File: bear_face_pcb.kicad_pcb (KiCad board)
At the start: 2 copper layers, 300 x 111.8 mm, 216 parts, among them J1 USB-C, J2 Conn_02x03_Odd_Even, SW1 RESET, U1 ATmega32U4-AU, U2 SRV05-4, Y1 16MHz

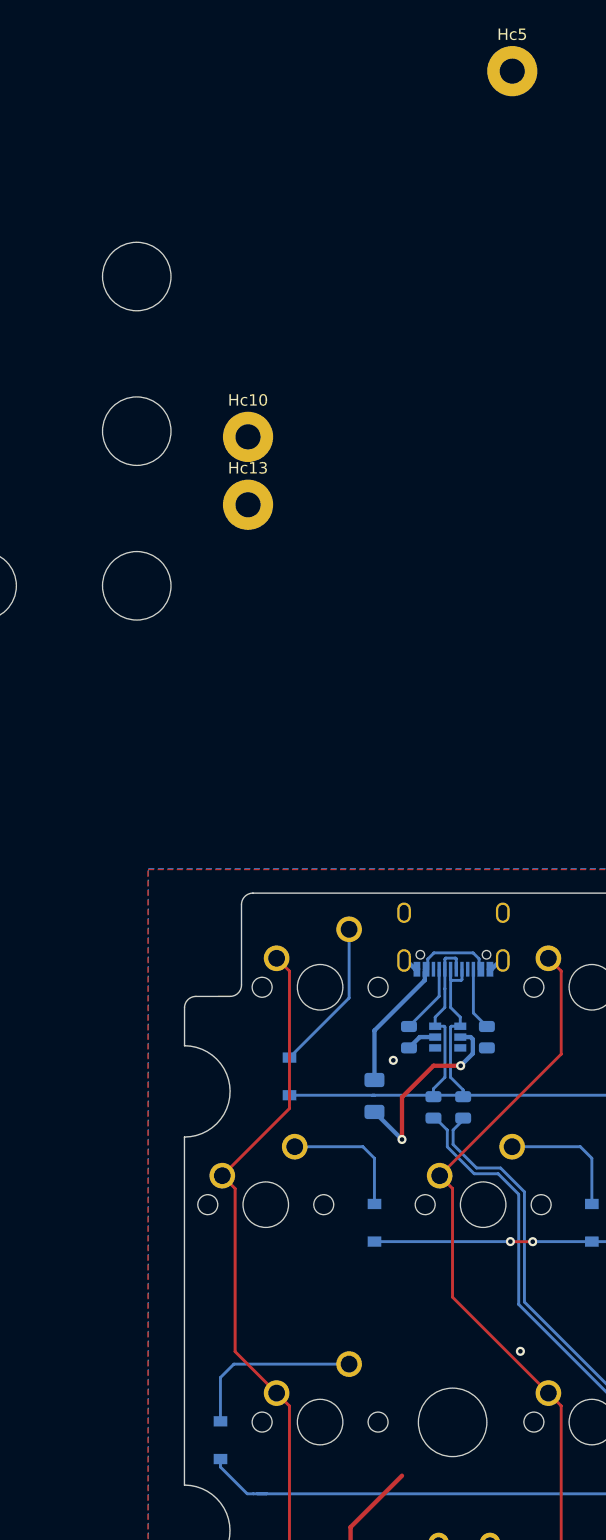
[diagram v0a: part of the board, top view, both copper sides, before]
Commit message: softened corners * mount holes still WIP
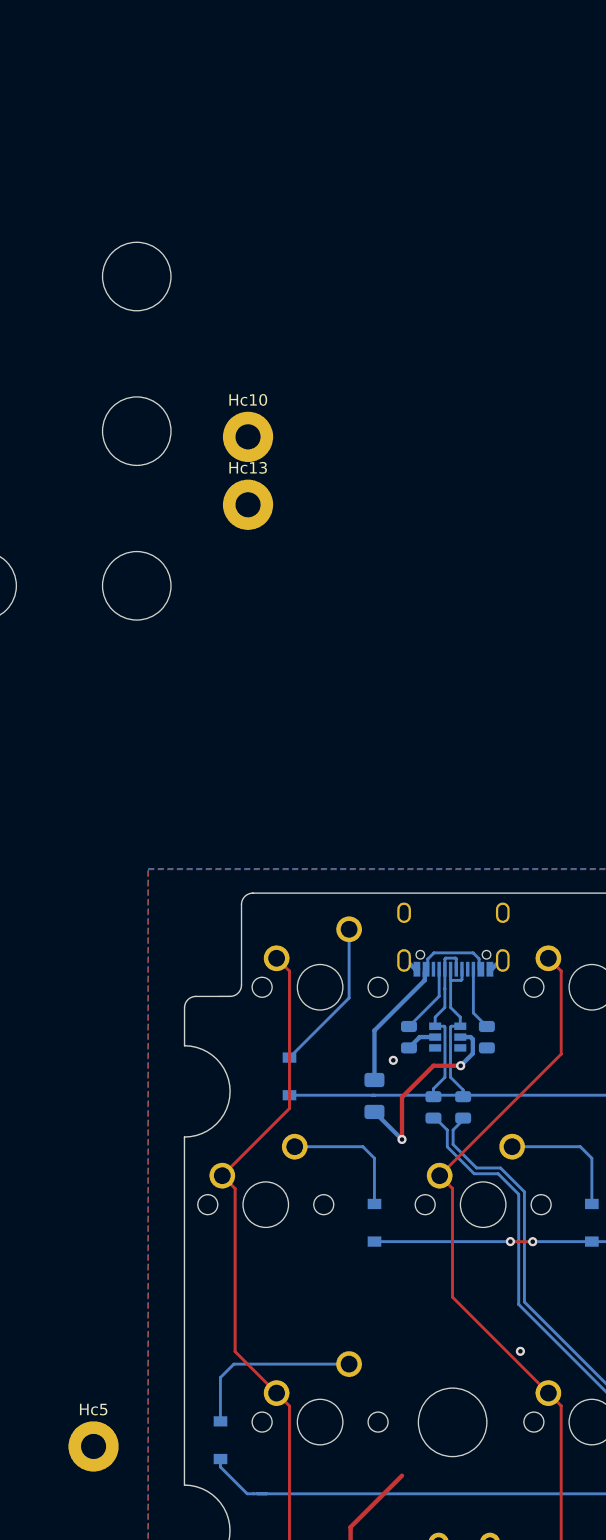
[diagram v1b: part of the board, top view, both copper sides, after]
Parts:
- moved Hc5 126.0 mm to (52.3, 118.1)
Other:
- board text removed: "USB CUTOUT"
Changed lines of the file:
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@@
   )
   (footprint "MountingHole:MountingHole_2.2mm_M2_Pad" (layer "F.Cu")
-    (at 89.037 -2.424)
+    (at 52.3494 118.0846)
     (descr "Mounting Hole 2.2mm, M2")
     (tags "mounting hole 2.2mm m2")
@@
     (fp_circle (center 0 0) (end 2.45 0)
       (stroke (width 0.05) (type solid)) (fill none) (layer "F.CrtYd"))
-    (pad "1" thru_hole circle (at 0 0) (size 4.4 4.4) (drill 2.2) (layers "*.Cu" "*.Mask")
+    (pad "1" thru_hole circle (at 0 0) (size 4.4 4.4) (drill 2.2) (layers "*.Cu" "B.Mask")
       (net 84 "GND") (pinfunction "Pin_1") (pintype "passive"))
   )
@@
     )
     (fp_line (start -4.468987 -5.094056) (end -4.468987 -3.612751)
-      (stroke (width 0.254001) (type solid)) (layer "B.SilkS"))
+      (stroke (width 0.254) (type solid)) (layer "B.SilkS"))
     (fp_line (start -4.468987 -1.375667) (end -4.468987 0.487249)
-      (stroke (width 0.254001) (type solid)) (layer "B.SilkS"))
+      (stroke (width 0.254) (type solid)) (layer "B.SilkS"))
     (fp_line (start 4.471019 -5.094056) (end -4.468987 -5.094056)
-      (stroke (width 0.254001) (type solid)) (layer "B.SilkS"))
+      (stroke (width 0.254) (type solid)) (layer "B.SilkS"))
     (fp_line (start 4.471019 -5.094056) (end 4.471019 -3.612395)
-      (stroke (width 0.254001) (type solid)) (layer "B.SilkS"))
+      (stroke (width 0.254) (type solid)) (layer "B.SilkS"))
     (fp_line (start 4.471019 -1.376022) (end 4.471019 0.487605)
-      (stroke (width 0.254001) (type solid)) (layer "B.SilkS"))
+      (stroke (width 0.254) (type solid)) (layer "B.SilkS"))
     (fp_circle (center -4.475032 2.75616) (end -4.445034 2.75616)
       (stroke (width 0.059995) (type solid)) (fill none) (layer "B.SilkS"))
     (fp_circle (center -2.899924 1.205664) (end -2.774956 1.205664)
-      (stroke (width 0.250013) (type solid)) (fill none) (layer "B.Fab"))
+      (stroke (width 0.250012) (type solid)) (fill none) (layer "B.Fab"))
     (fp_circle (center 2.899924 1.205664) (end 3.024892 1.205664)
-      (stroke (width 0.250013) (type solid)) (fill none) (layer "B.Fab"))
+      (stroke (width 0.250012) (type solid)) (fill none) (layer "B.Fab"))
     (pad "" np_thru_hole circle (at -2.899924 1.205664) (size 0.750013 0.750013) (drill 0.750013) (layers "*.Cu" "*.Mask"))
     (pad "" np_thru_hole circle (at 2.899924 1.205664) (size 0.750013 0.750013) (drill 0.750013) (layers "*.Cu" "*.Mask"))
@@
     )
   )
-  (gr_line (start 364.2995 65.94475) (end 364.2995 185.00725)
-    (stroke (width 0.15) (type solid)) (layer "Cmts.User"))
-  (gr_line (start 56.3245 185.00725) (end 364.2995 185.00725)
-    (stroke (width 0.15) (type solid)) (layer "Cmts.User"))
   (gr_line (start 79.68 69.866) (end 88.062 69.866)
     (stroke (width 0.15) (type solid)) (layer "Cmts.User"))
-  (gr_line (start 56.3245 65.94475) (end 56.3245 185.00725)
-    (stroke (width 0.15) (type solid)) (layer "Cmts.User"))
-  (gr_line (start 56.3245 65.94475) (end 364.2995 65.94475)
-    (stroke (width 0.15) (type solid)) (layer "Cmts.User"))
-  (gr_line (start 88.182 68.676) (end 90.212 63.376)
-    (stroke (width 0.15) (type solid)) (layer "Cmts.User"))
   (gr_line (start 65.361515 181.447) (end 355.240091 181.447)
     (stroke (width 0.12) (type solid)) (layer "Edge.Cuts"))
@@
     (effects (font (size 1.5 1.5) (thickness 0.3)) (justify mirror))
   )
-  (gr_text "USB CUTOUT" (at 95.002 63.436) (layer "Cmts.User")
-    (effects (font (size 1 1) (thickness 0.15)))
-  )
   (gr_text "CASE OUTLINE" (at 61.512 64.976) (layer "Cmts.User")

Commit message: changing mount holes to unplated WIP
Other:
- outline, holes or cut-outs redrawn
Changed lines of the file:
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@@
   (gr_line (start 354.319106 69.601002) (end 66.312 69.601501)
     (stroke (width 0.12) (type solid)) (layer "Edge.Cuts"))
-  (gr_line (start 60.312 90.976) (end 60.312 121.472447)
+  (gr_line (start 60.312 91.201) (end 60.312 121.226)
     (stroke (width 0.12) (type solid)) (layer "Edge.Cuts"))
-  (gr_line (start 360.312 79.651002) (end 360.312 82.976)
+  (gr_line (start 360.312 79.651002) (end 360.308814 82.725999)
     (stroke (width 0.12) (type solid)) (layer "Edge.Cuts"))
-  (gr_line (start 360.32 90.976) (end 360.3112 121.476)
+  (gr_line (start 360.312 91.222777) (end 360.312 121.236)
     (stroke (width 0.12) (type solid)) (layer "Edge.Cuts"))
-  (gr_line (start 60.312 148.479) (end 60.3128 159.5506)
+  (gr_line (start 60.313777 148.727777) (end 60.312001 159.300999)
     (stroke (width 0.12) (type solid)) (layer "Edge.Cuts"))
-  (gr_arc (start 60.319106 82.976) (mid 64.312005 86.979553) (end 60.312 90.976006)
+  (gr_arc (start 60.563658 83.001106) (mid 64.294852 86.976831) (end 60.562 90.950999)
     (stroke (width 0.12) (type solid)) (layer "Edge.Cuts"))
-  (gr_arc (start 360.312 90.976) (mid 356.312 86.976) (end 360.312 82.976)
+  (gr_arc (start 360.065012 90.975999) (mid 356.304383 86.977504) (end 360.06201 82.976188)
     (stroke (width 0.12) (type solid)) (layer "Edge.Cuts"))
   (gr_arc (start 360.32 176.397485) (mid 358.821399 179.969862) (end 355.240091 181.447)
     (stroke (width 0.12) (type solid)) (layer "Edge.Cuts"))
+  (gr_arc (start 360.064933 167.559147) (mid 360.246694 167.634302) (end 360.322 167.816)
+    (stroke (width 0.12) (type default)) (layer "Edge.Cuts"))
+  (gr_arc (start 60.313777 129.718716) (mid 60.387 129.541939) (end 60.563777 129.468716)
+    (stroke (width 0.12) (type default)) (layer "Edge.Cuts"))
+  (gr_arc (start 60.313777 148.727777) (mid 60.387 148.551) (end 60.563777 148.477777)
+    (stroke (width 0.12) (type default)) (layer "Edge.Cuts"))
+  (gr_arc (start 360.312 159.334239) (mid 360.236845 159.516) (end 360.055147 159.591306)
+    (stroke (width 0.12) (type default)) (layer "Edge.Cuts"))
   (gr_arc (start 354.319106 69.601002) (mid 355.026208 69.893897) (end 355.319106 70.601002)
     (stroke (width 0.12) (type default)) (layer "Edge.Cuts"))
-  (gr_line (start 360.3112 129.476) (end 360.3112 159.576)
+  (gr_arc (start 360.312 121.236) (mid 360.238853 121.412915) (end 360.062 121.486214)
+    (stroke (width 0.12) (type default)) (layer "Edge.Cuts"))
+  (gr_line (start 360.312 129.716) (end 360.312 159.339085)
     (stroke (width 0.12) (type default)) (layer "Edge.Cuts"))
   (gr_arc (start 356.319106 78.65) (mid 355.611995 78.357109) (end 355.319106 77.65)
+    (stroke (width 0.12) (type default)) (layer "Edge.Cuts"))
+  (gr_arc (start 60.562 121.476) (mid 60.385223 121.402777) (end 60.312 121.226)
+    (stroke (width 0.12) (type default)) (layer "Edge.Cuts"))
+  (gr_arc (start 360.065012 90.976) (mid 360.239646 91.048204) (end 360.312 91.222777)
     (stroke (width 0.12) (type default)) (layer "Edge.Cuts"))
   (gr_arc (start 65.361515 181.447826) (mid 61.789129 179.949227) (end 60.312 176.367917)
@@
   (gr_line (start 355.319106 77.65) (end 355.319106 70.601002)
     (stroke (width 0.12) (type default)) (layer "Edge.Cuts"))
-  (gr_arc (start 360.3112 167.576) (mid 356.3112 163.576) (end 360.3112 159.576)
+  (gr_arc (start 360.064933 167.559146) (mid 356.320451 163.580833) (end 360.055286 159.593462)
     (stroke (width 0.12) (type solid)) (layer "Edge.Cuts"))
   (gr_line (start 359.312 78.651002) (end 356.319106 78.65)
@@
   (gr_arc (start 65.312 77.650499) (mid 65.019107 78.357606) (end 64.312 78.650499)
     (stroke (width 0.12) (type default)) (layer "Edge.Cuts"))
-  (gr_arc (start 60.312 140.479) (mid 64.312 144.479) (end 60.312 148.479)
+  (gr_arc (start 60.5634 140.4802) (mid 64.318695 144.478811) (end 60.563777 148.477776)
     (stroke (width 0.12) (type solid)) (layer "Edge.Cuts"))
   (gr_arc (start 60.319106 79.651501) (mid 60.611999 78.944396) (end 61.319106 78.651501)
@@
   (gr_arc (start 65.312 70.601501) (mid 65.604893 69.894394) (end 66.312 69.601501)
     (stroke (width 0.12) (type default)) (layer "Edge.Cuts"))
+  (gr_arc (start 360.308814 82.725999) (mid 360.23673 82.901717) (end 360.06201 82.976188)
+    (stroke (width 0.12) (type default)) (layer "Edge.Cuts"))
   (gr_arc (start 359.312 78.651002) (mid 360.019106 78.943895) (end 360.312 79.651002)
+    (stroke (width 0.12) (type default)) (layer "Edge.Cuts"))
+  (gr_arc (start 60.569106 82.999223) (mid 60.392329 82.926) (end 60.319106 82.749223)
+    (stroke (width 0.12) (type default)) (layer "Edge.Cuts"))
+  (gr_arc (start 60.562001 159.550999) (mid 60.385224 159.477776) (end 60.312001 159.300999)
     (stroke (width 0.12) (type default)) (layer "Edge.Cuts"))
   (gr_line (start 64.312 78.650499) (end 61.319106 78.651501)
     (stroke (width 0.12) (type default)) (layer "Edge.Cuts"))
-  (gr_line (start 60.312 167.5506) (end 60.312 176.367917)
+  (gr_line (start 60.312 167.801) (end 60.312 176.367917)
+    (stroke (width 0.12) (type default)) (layer "Edge.Cuts"))
+  (gr_arc (start 60.563777 140.474223) (mid 60.387 140.401) (end 60.313777 140.224223)
     (stroke (width 0.12) (type default)) (layer "Edge.Cuts"))
   (gr_line (start 65.312 70.601501) (end 65.312 77.650499)
     (stroke (width 0.12) (type default)) (layer "Edge.Cuts"))
-  (gr_arc (start 60.312 121.472447) (mid 64.304899 125.476) (end 60.304894 129.472453)
+  (gr_arc (start 60.56189 121.477707) (mid 64.307872 125.484918) (end 60.537 129.468716)
     (stroke (width 0.12) (type solid)) (layer "Edge.Cuts"))
-  (gr_line (start 60.319106 79.651501) (end 60.319106 82.976)
+  (gr_line (start 60.319106 79.651501) (end 60.319106 82.749223)
     (stroke (width 0.12) (type default)) (layer "Edge.Cuts"))
-  (gr_line (start 360.32 167.576) (end 360.32 176.397485)
+  (gr_line (start 360.322 167.816) (end 360.32 176.397485)
     (stroke (width 0.12) (type default)) (layer "Edge.Cuts"))
-  (gr_line (start 60.312 129.472453) (end 60.312 140.479)
+  (gr_line (start 60.313777 129.718716) (end 60.313777 140.224223)
     (stroke (width 0.12) (type default)) (layer "Edge.Cuts"))
-  (gr_arc (start 360.3112 129.476) (mid 356.3112 125.476) (end 360.3112 121.476)
+  (gr_arc (start 360.061786 129.466) (mid 360.238701 129.539147) (end 360.312 129.716)
+    (stroke (width 0.12) (type default)) (layer "Edge.Cuts"))
+  (gr_arc (start 360.061786 129.465999) (mid 356.313413 125.4759) (end 360.061986 121.485988)
     (stroke (width 0.12) (type solid)) (layer "Edge.Cuts"))
-  (gr_arc (start 60.3128 159.5506) (mid 64.3128 163.5506) (end 60.3128 167.5506)
+  (gr_arc (start 60.562051 159.550203) (mid 64.320954 163.550626) (end 60.562 167.551)
     (stroke (width 0.12) (type solid)) (layer "Edge.Cuts"))
+  (gr_arc (start 60.312 167.801) (mid 60.385223 167.624223) (end 60.562 167.551)
+    (stroke (width 0.12) (type default)) (layer "Edge.Cuts"))
+  (gr_arc (start 60.312 91.201) (mid 60.385223 91.024223) (end 60.562 90.951)
+    (stroke (width 0.12) (type default)) (layer "Edge.Cuts"))
   (gr_text "bear_face v3.1c\ndesigned by /u/chemicalwill" (at 218.312 170.688) (layer "B.SilkS")
     (effects (font (size 1.5 1.5) (thickness 0.3)) (justify mirror))
